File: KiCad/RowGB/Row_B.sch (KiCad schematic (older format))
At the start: 37 parts, among them U201 RGB_WS2811, U202 RGB_WS2811, U203 RGB_WS2811, U204 RGB_WS2811, U205 RGB_WS2811, U206 RGB_WS2811, U207 RGB_WS2811, U208 RGB_WS2811, U209 RGB_WS2811, U210 RGB_WS2811, U211 RGB_WS2811, U212 RGB_WS2811, U213 RGB_WS2811, U214 RGB_WS2811, U215 RGB_WS2811, U216 RGB_WS2811

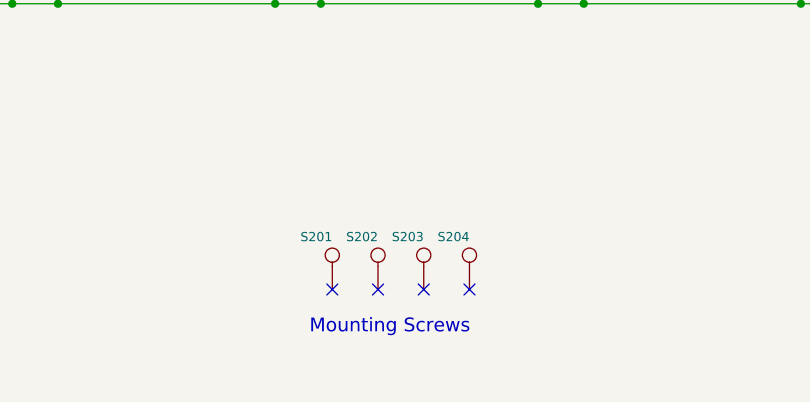
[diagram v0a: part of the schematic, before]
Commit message: TiM : Need to add legend for stacking connectors.
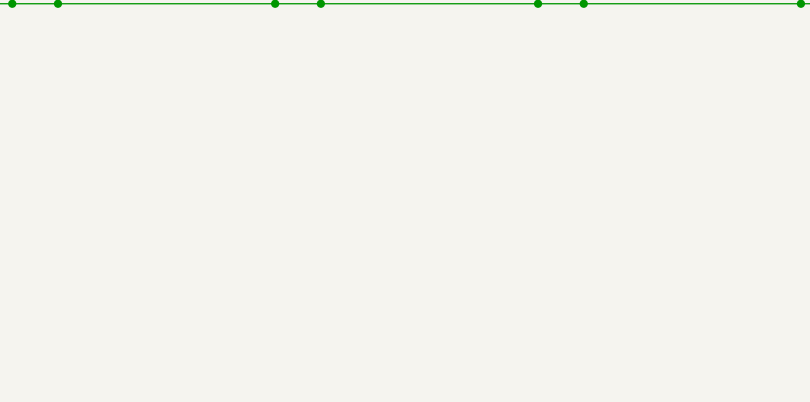
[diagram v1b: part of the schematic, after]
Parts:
- removed S201, S202, S203, S204: CONN_1, Screw, symbol CONN_1
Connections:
- no-connect marks 20 -> 16
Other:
- note removed: "Mounting Screws"
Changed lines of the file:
@@
-EESchema Schematic File Version 2  date Tuesday 12 February 2013 12:06:40 AM IST
+EESchema Schematic File Version 2  date 2/13/2013 1:59:50 PM
 LIBS:RowGB_sym
 LIBS:power
@@
 Sheet 8 9
 Title "TiM - The Intelligent Matrix"
-Date "11 feb 2013"
+Date "13 feb 2013"
 Rev ""
 Comp "WyoLum"
@@
 	1    0    0    -1
 $EndComp
-$Comp
-L CONN_1 S201
-U 1 1 5118AB7C
-P 5300 6650
-F 0 "S201" V 5380 6650 40  0000 L CNN
-F 1 "CONN_1" H 5300 6705 30  0001 C CNN
-F 2 "Screw" H 5300 6805 30  0001 C CNN
-	1    5300 6650
-	0    -1   -1   0
-$EndComp
-$Comp
-L CONN_1 S202
-U 1 1 5118AB71
-P 5500 6650
-F 0 "S202" V 5580 6650 40  0000 L CNN
-F 1 "CONN_1" H 5500 6705 30  0001 C CNN
-F 2 "Screw" H 5500 6805 30  0001 C CNN
-	1    5500 6650
-	0    -1   -1   0
-$EndComp
-$Comp
-L CONN_1 S203
-U 1 1 5118AB6B
-P 5700 6650
-F 0 "S203" V 5780 6650 40  0000 L CNN
-F 1 "CONN_1" H 5700 6705 30  0001 C CNN
-F 2 "Screw" H 5700 6805 30  0001 C CNN
-	1    5700 6650
-	0    -1   -1   0
-$EndComp
-$Comp
-L CONN_1 S204
-U 1 1 51189822
-P 5900 6650
-F 0 "S204" V 5980 6650 40  0000 L CNN
-F 1 "CONN_1" H 5900 6705 30  0001 C CNN
-F 2 "Screw" H 5900 6805 30  0001 C CNN
-	1    5900 6650
-	0    -1   -1   0
-$EndComp
-NoConn ~ 5300 6800
-NoConn ~ 5500 6800
-NoConn ~ 5700 6800
-NoConn ~ 5900 6800
-Text Notes 5200 7000 0    60   ~ 0
-Mounting Screws
 Text Label 1250 6350 0    60   ~ 0
 5V
